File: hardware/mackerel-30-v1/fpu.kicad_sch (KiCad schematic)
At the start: 11 parts, among them U11 MC68882

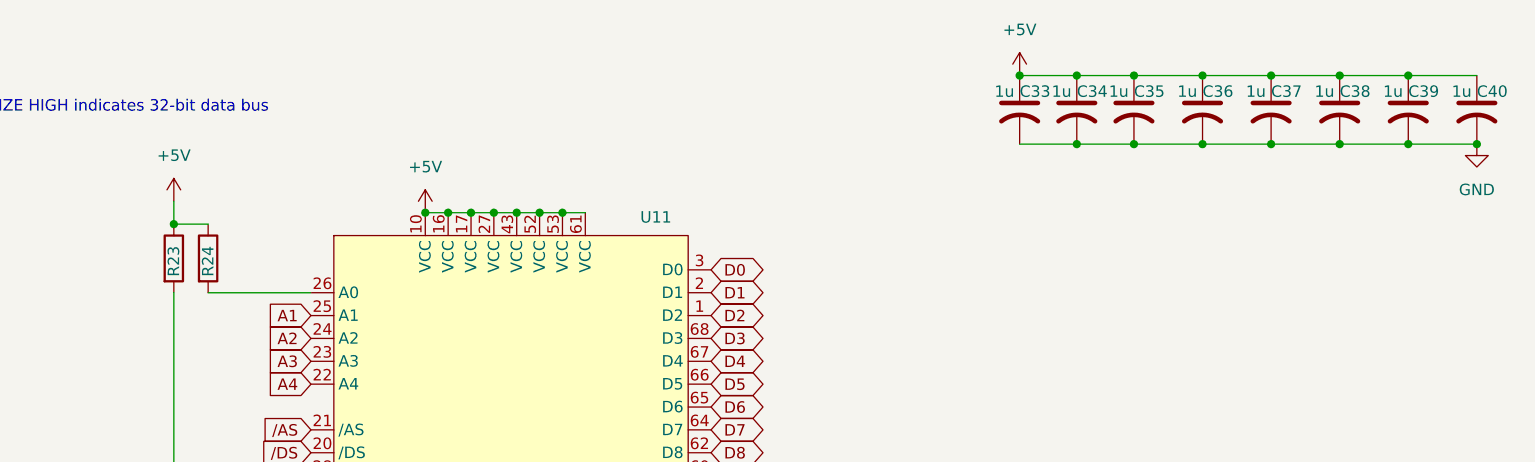
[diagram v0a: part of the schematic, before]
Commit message: SIMM and data buffers mostly routed
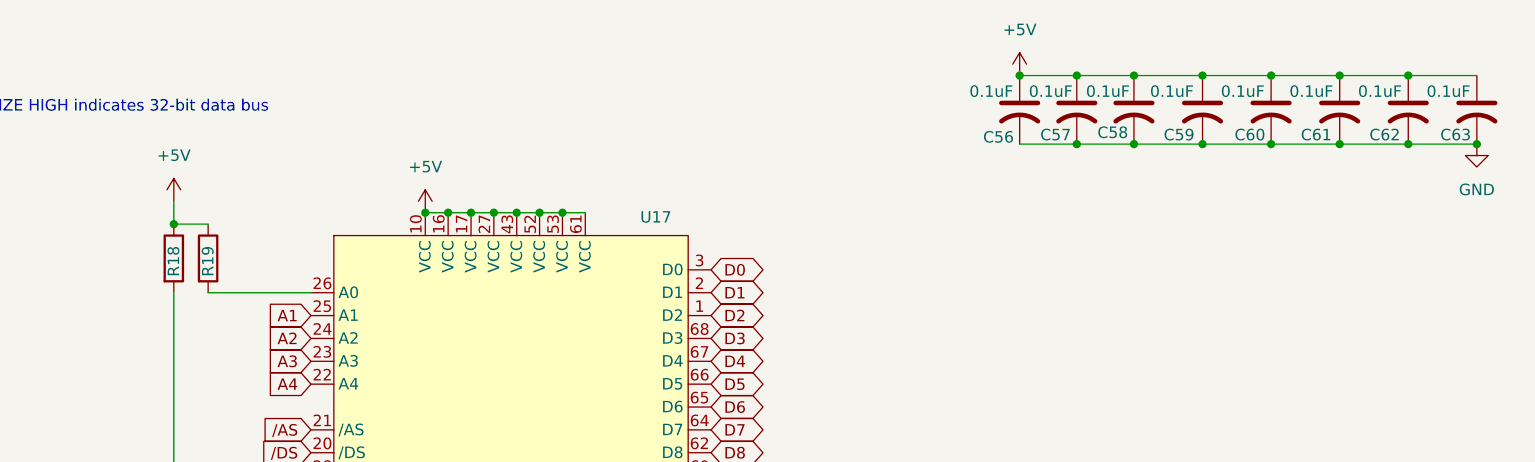
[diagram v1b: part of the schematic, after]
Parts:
- C56: renamed from C33; value 1u -> 0.1uF; footprint Capacitor_SMD:C_0805_2012Metric_Pad1.18x1.45mm_HandSolder -> Capacitor_SMD:C_1206_3216Metric_Pad1.33x1.80mm_HandSolder
- C57: renamed from C34; value 1u -> 0.1uF; footprint Capacitor_SMD:C_0805_2012Metric_Pad1.18x1.45mm_HandSolder -> Capacitor_SMD:C_1206_3216Metric_Pad1.33x1.80mm_HandSolder
- C58: renamed from C35; value 1u -> 0.1uF; footprint Capacitor_SMD:C_0805_2012Metric_Pad1.18x1.45mm_HandSolder -> Capacitor_SMD:C_1206_3216Metric_Pad1.33x1.80mm_HandSolder
- C59: renamed from C36; value 1u -> 0.1uF; footprint Capacitor_SMD:C_0805_2012Metric_Pad1.18x1.45mm_HandSolder -> Capacitor_SMD:C_1206_3216Metric_Pad1.33x1.80mm_HandSolder
- C60: renamed from C37; value 1u -> 0.1uF; footprint Capacitor_SMD:C_0805_2012Metric_Pad1.18x1.45mm_HandSolder -> Capacitor_SMD:C_1206_3216Metric_Pad1.33x1.80mm_HandSolder
- C61: renamed from C38; value 1u -> 0.1uF; footprint Capacitor_SMD:C_0805_2012Metric_Pad1.18x1.45mm_HandSolder -> Capacitor_SMD:C_1206_3216Metric_Pad1.33x1.80mm_HandSolder
- C62: renamed from C39; value 1u -> 0.1uF; footprint Capacitor_SMD:C_0805_2012Metric_Pad1.18x1.45mm_HandSolder -> Capacitor_SMD:C_1206_3216Metric_Pad1.33x1.80mm_HandSolder
- C63: renamed from C40; value 1u -> 0.1uF; footprint Capacitor_SMD:C_0805_2012Metric_Pad1.18x1.45mm_HandSolder -> Capacitor_SMD:C_1206_3216Metric_Pad1.33x1.80mm_HandSolder
- R18: renamed from R23; footprint Resistor_THT:R_Axial_DIN0207_L6.3mm_D2.5mm_P7.62mm_Horizontal -> Resistor_SMD:R_1206_3216Metric_Pad1.30x1.75mm_HandSolder
- R19: renamed from R24; footprint Resistor_THT:R_Axial_DIN0207_L6.3mm_D2.5mm_P7.62mm_Horizontal -> Resistor_SMD:R_1206_3216Metric_Pad1.30x1.75mm_HandSolder
- renumbered U11 to U17
